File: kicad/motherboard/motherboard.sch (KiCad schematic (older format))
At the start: 21 parts, among them J1 DB37_Female, J10 DB37_Female, J11 DB37_Female, J12 Barrel_Jack, J13 TSR 1-2433, J2 DB37_Female, J3 DB37_Female, J4 DB37_Female, J5 DB37_Female, J6 DB25_Female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

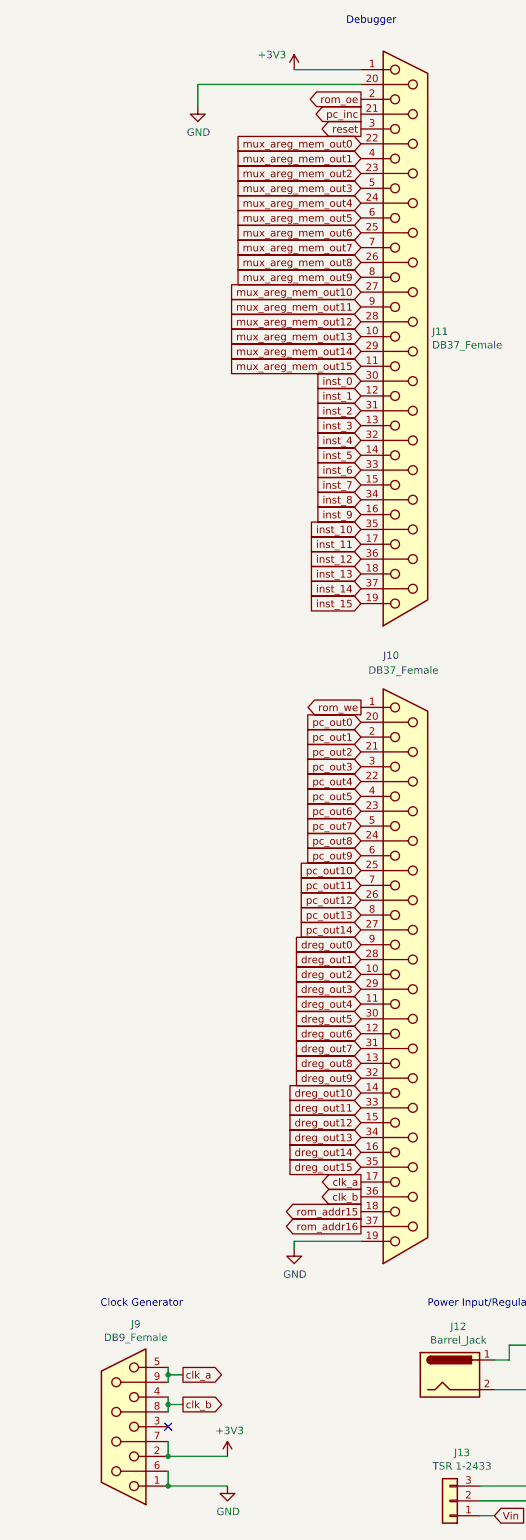
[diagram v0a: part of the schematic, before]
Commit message: Added clock output enable signal to motherboard debugger. Updated component library.
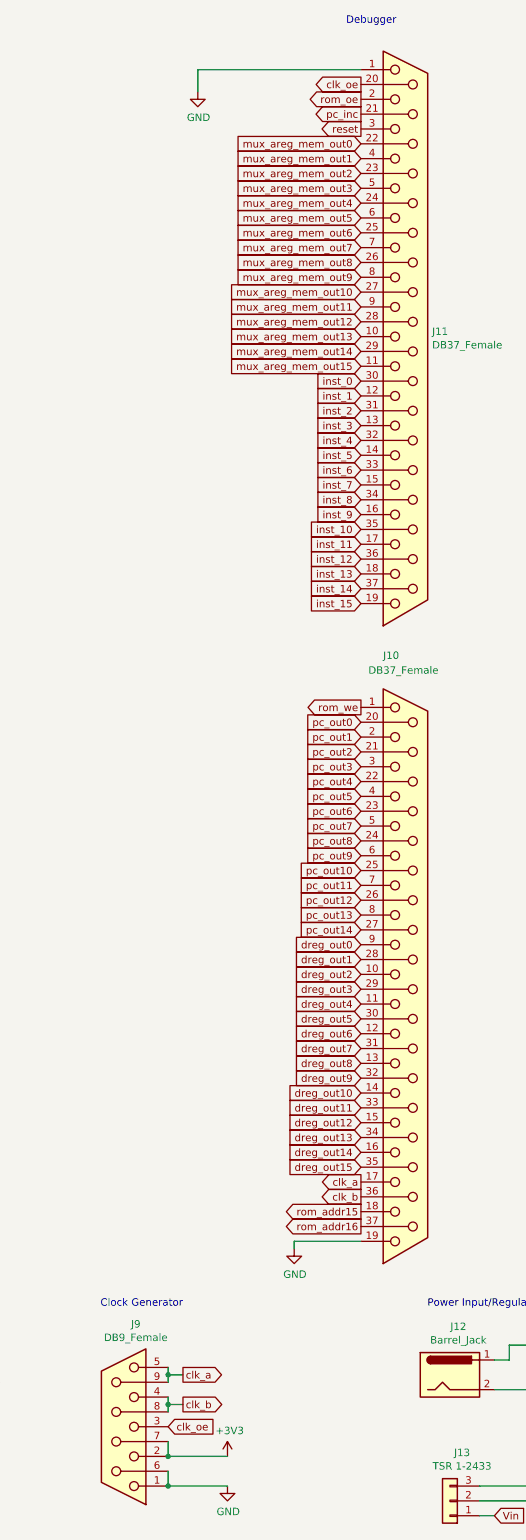
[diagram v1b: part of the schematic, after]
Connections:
- net +3V3: no longer J11.1
- net GND: now also J11.1; no longer J11.20
- net clk_oe: now reaches J9.3
- net clk_oe: now also J11.20
- no-connect marks 8 -> 7
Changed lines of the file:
@@
 	6500 10500 6900 10500
 Connection ~ 6500 10500
-NoConn ~ 6500 10100
 $Sheet
 S 11250 6050 750  3350
@@
 L power:GND #PWR052
 U 1 1 5E99FE8F
-P 6700 1200
-F 0 "#PWR052" H 6700 950 50  0001 C CNN
-F 1 "GND" H 6705 1027 50  0000 C CNN
-F 2 "" H 6700 1200 50  0001 C CNN
-F 3 "" H 6700 1200 50  0001 C CNN
-	1    6700 1200
-	1    0    0    -1
-$EndComp
-Wire Wire Line
-	7800 950  7350 950
-$Comp
-L power:+3V3 #PWR051
-U 1 1 5E9A1A48
-P 7350 950
-F 0 "#PWR051" H 7350 800 50  0001 C CNN
-F 1 "+3V3" H 7200 1050 50  0000 C CNN
-F 2 "" H 7350 950 50  0001 C CNN
-F 3 "" H 7350 950 50  0001 C CNN
-	1    7350 950
+P 6700 1100
+F 0 "#PWR052" H 6700 850 50  0001 C CNN
+F 1 "GND" H 6705 927 50  0000 C CNN
+F 2 "" H 6700 1100 50  0001 C CNN
+F 3 "" H 6700 1100 50  0001 C CNN
+	1    6700 1100
 	1    0    0    -1
 $EndComp
@@
 	7800 8850 7350 8850
 Wire Wire Line
-	7800 1050 6700 1050
-Wire Wire Line
-	6700 1050 6700 1200
+	7800 950  6700 950
+Wire Wire Line
+	6700 950  6700 1100
+Text GLabel 6500 10100 2    50   Input ~ 0
+clk_oe
+Text GLabel 7800 1050 0    50   Output ~ 0
+clk_oe
 $EndSCHEMATC

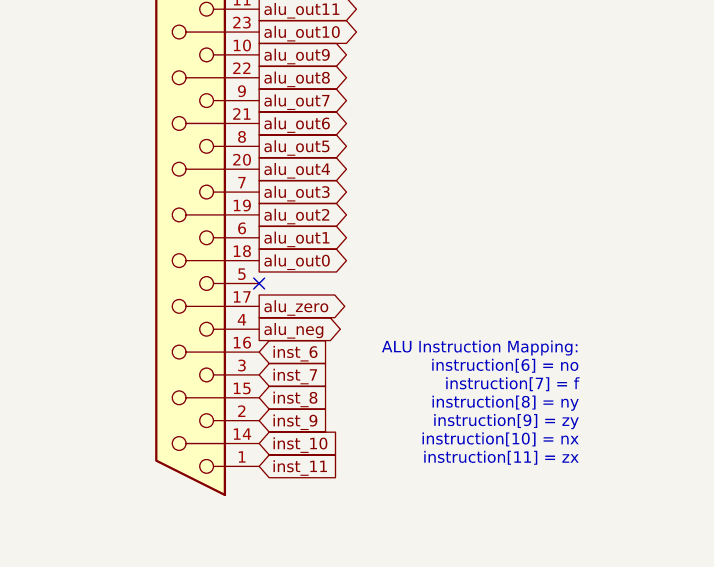
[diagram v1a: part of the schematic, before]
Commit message: ALU schematic, layout, routing complete. Associated motherboardmod. Also added Load LED to register and program counter boards.
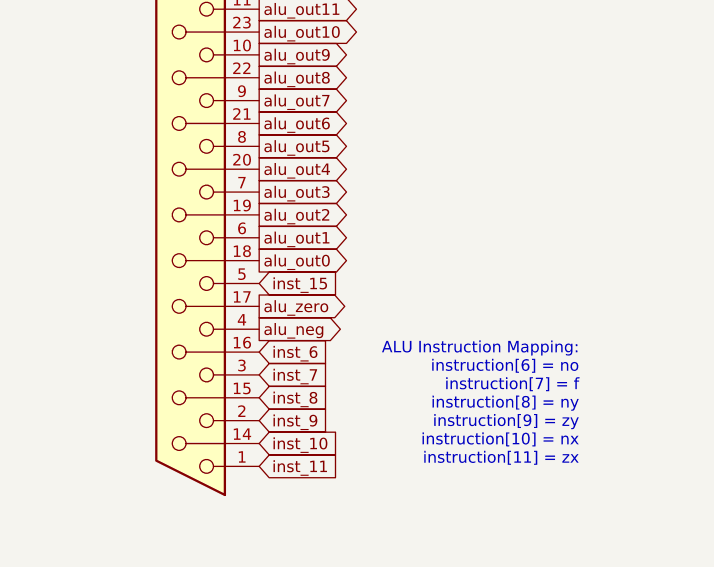
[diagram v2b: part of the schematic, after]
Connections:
- net inst_15: now also J6.5
- no-connect marks 7 -> 6
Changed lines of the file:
@@
 	1    0    0    -1
 $EndComp
-NoConn ~ 1750 6900
 $Comp
 L Device:CP1 C2
@@
 Text GLabel 7800 1050 0    50   Output ~ 0
 clk_oe
+Text GLabel 1750 6900 2    50   Input ~ 0
+inst_15
 $EndSCHEMATC
